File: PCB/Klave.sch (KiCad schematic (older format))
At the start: 78 parts, among them J1 6P6C, J2 OLED, SW0 Reset, SW1 0:0, SW10 1:3, SW11 1:4, SW12 1:5, SW13 2:0, SW14 2:1, SW15 2:2, SW16 2:3, SW17 2:4, SW18 2:5, SW19 3:0, SW2 0:1, SW20 3:1, SW21 3:2, SW22 3:3, SW23 3:4, SW24 3:5, SW26 4:1, SW27 4:2, SW28 4:3, SW29 4:4, SW3 0:2, SW30 4:5, SW35 5:4, SW36 5:5, SW4 0:3, SW5 0:4, SW6 0:5, SW7 1:0, SW8 1:1, SW9 1:2, U1 ProMicro

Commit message: Rename switch files
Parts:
- SW1, SW10, SW11, SW12, SW13, SW14, SW15, SW16, SW17, SW18, SW19, SW2, SW20, SW21, SW22, SW23, SW24, SW26, SW27, SW28, SW29, SW3, SW30, SW35, SW36, SW4, SW5, SW6, SW7, SW8, SW9: footprint KlaveLib:Kailh_MX_Socket -> KlaveLib:SW_Socket_MX
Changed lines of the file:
@@
 F 0 "SW2" H 7550 1900 50  0000 C CNN
 F 1 "0:1" H 7550 1600 50  0000 C CNB
-F 2 "KlaveLib:Kailh_MX_Socket" H 7550 1900 50  0001 C CNN
+F 2 "KlaveLib:SW_Socket_MX" H 7550 1900 50  0001 C CNN
 F 3 "~" H 7550 1900 50  0001 C CNN
 	1    7550 1700
@@
 F 0 "SW3" H 8250 1900 50  0000 C CNN
 F 1 "0:2" H 8250 1600 50  0000 C CNB
-F 2 "KlaveLib:Kailh_MX_Socket" H 8250 1900 50  0001 C CNN
+F 2 "KlaveLib:SW_Socket_MX" H 8250 1900 50  0001 C CNN
 F 3 "~" H 8250 1900 50  0001 C CNN
 	1    8250 1700
@@
 F 0 "SW4" H 8950 1900 50  0000 C CNN
 F 1 "0:3" H 8950 1600 50  0000 C CNB
-F 2 "KlaveLib:Kailh_MX_Socket" H 8950 1900 50  0001 C CNN
+F 2 "KlaveLib:SW_Socket_MX" H 8950 1900 50  0001 C CNN
 F 3 "~" H 8950 1900 50  0001 C CNN
 	1    8950 1700
@@
 F 0 "SW5" H 9650 1900 50  0000 C CNN
 F 1 "0:4" H 9650 1600 50  0000 C CNB
-F 2 "KlaveLib:Kailh_MX_Socket" H 9650 1900 50  0001 C CNN
+F 2 "KlaveLib:SW_Socket_MX" H 9650 1900 50  0001 C CNN
 F 3 "~" H 9650 1900 50  0001 C CNN
 	1    9650 1700
@@
 F 0 "SW6" H 10350 1900 50  0000 C CNN
 F 1 "0:5" H 10350 1600 50  0000 C CNB
-F 2 "KlaveLib:Kailh_MX_Socket" H 10350 1900 50  0001 C CNN
+F 2 "KlaveLib:SW_Socket_MX" H 10350 1900 50  0001 C CNN
 F 3 "~" H 10350 1900 50  0001 C CNN
 	1    10350 1700
@@
 F 0 "SW24" H 10350 3550 50  0000 C CNN
 F 1 "3:5" H 10350 3250 50  0000 C CNB
-F 2 "KlaveLib:Kailh_MX_Socket" H 10350 3550 50  0001 C CNN
+F 2 "KlaveLib:SW_Socket_MX" H 10350 3550 50  0001 C CNN
 F 3 "~" H 10350 3550 50  0001 C CNN
 	1    10350 3350
@@
 F 0 "SW12" H 10350 2450 50  0000 C CNN
 F 1 "1:5" H 10350 2150 50  0000 C CNB
-F 2 "KlaveLib:Kailh_MX_Socket" H 10350 2450 50  0001 C CNN
+F 2 "KlaveLib:SW_Socket_MX" H 10350 2450 50  0001 C CNN
 F 3 "~" H 10350 2450 50  0001 C CNN
 	1    10350 2250
@@
 F 0 "SW23" H 9650 3550 50  0000 C CNN
 F 1 "3:4" H 9650 3250 50  0000 C CNB
-F 2 "KlaveLib:Kailh_MX_Socket" H 9650 3550 50  0001 C CNN
+F 2 "KlaveLib:SW_Socket_MX" H 9650 3550 50  0001 C CNN
 F 3 "~" H 9650 3550 50  0001 C CNN
 	1    9650 3350
@@
 F 0 "SW17" H 9650 3000 50  0000 C CNN
 F 1 "2:4" H 9650 2700 50  0000 C CNB
-F 2 "KlaveLib:Kailh_MX_Socket" H 9650 3000 50  0001 C CNN
+F 2 "KlaveLib:SW_Socket_MX" H 9650 3000 50  0001 C CNN
 F 3 "~" H 9650 3000 50  0001 C CNN
 	1    9650 2800
@@
 F 0 "SW11" H 9650 2450 50  0000 C CNN
 F 1 "1:4" H 9650 2150 50  0000 C CNB
-F 2 "KlaveLib:Kailh_MX_Socket" H 9650 2450 50  0001 C CNN
+F 2 "KlaveLib:SW_Socket_MX" H 9650 2450 50  0001 C CNN
 F 3 "~" H 9650 2450 50  0001 C CNN
 	1    9650 2250
@@
 F 0 "SW22" H 8950 3550 50  0000 C CNN
 F 1 "3:3" H 8950 3250 50  0000 C CNB
-F 2 "KlaveLib:Kailh_MX_Socket" H 8950 3550 50  0001 C CNN
+F 2 "KlaveLib:SW_Socket_MX" H 8950 3550 50  0001 C CNN
 F 3 "~" H 8950 3550 50  0001 C CNN
 	1    8950 3350
@@
 F 0 "SW16" H 8950 3000 50  0000 C CNN
 F 1 "2:3" H 8950 2700 50  0000 C CNB
-F 2 "KlaveLib:Kailh_MX_Socket" H 8950 3000 50  0001 C CNN
+F 2 "KlaveLib:SW_Socket_MX" H 8950 3000 50  0001 C CNN
 F 3 "~" H 8950 3000 50  0001 C CNN
 	1    8950 2800
@@
 F 0 "SW10" H 8950 2450 50  0000 C CNN
 F 1 "1:3" H 8950 2150 50  0000 C CNB
-F 2 "KlaveLib:Kailh_MX_Socket" H 8950 2450 50  0001 C CNN
+F 2 "KlaveLib:SW_Socket_MX" H 8950 2450 50  0001 C CNN
 F 3 "~" H 8950 2450 50  0001 C CNN
 	1    8950 2250
@@
 F 0 "SW21" H 8250 3550 50  0000 C CNN
 F 1 "3:2" H 8250 3250 50  0000 C CNB
-F 2 "KlaveLib:Kailh_MX_Socket" H 8250 3550 50  0001 C CNN
+F 2 "KlaveLib:SW_Socket_MX" H 8250 3550 50  0001 C CNN
 F 3 "~" H 8250 3550 50  0001 C CNN
 	1    8250 3350
@@
 F 0 "SW15" H 8250 3000 50  0000 C CNN
 F 1 "2:2" H 8250 2700 50  0000 C CNB
-F 2 "KlaveLib:Kailh_MX_Socket" H 8250 3000 50  0001 C CNN
+F 2 "KlaveLib:SW_Socket_MX" H 8250 3000 50  0001 C CNN
 F 3 "~" H 8250 3000 50  0001 C CNN
 	1    8250 2800
@@
 F 0 "SW20" H 7550 3550 50  0000 C CNN
 F 1 "3:1" H 7550 3250 50  0000 C CNB
-F 2 "KlaveLib:Kailh_MX_Socket" H 7550 3550 50  0001 C CNN
+F 2 "KlaveLib:SW_Socket_MX" H 7550 3550 50  0001 C CNN
 F 3 "~" H 7550 3550 50  0001 C CNN
 	1    7550 3350
@@
 F 0 "SW14" H 7550 3000 50  0000 C CNN
 F 1 "2:1" H 7550 2700 50  0000 C CNB
-F 2 "KlaveLib:Kailh_MX_Socket" H 7550 3000 50  0001 C CNN
+F 2 "KlaveLib:SW_Socket_MX" H 7550 3000 50  0001 C CNN
 F 3 "~" H 7550 3000 50  0001 C CNN
 	1    7550 2800
@@
 F 0 "SW8" H 7550 2450 50  0000 C CNN
 F 1 "1:1" H 7550 2150 50  0000 C CNB
-F 2 "KlaveLib:Kailh_MX_Socket" H 7550 2450 50  0001 C CNN
+F 2 "KlaveLib:SW_Socket_MX" H 7550 2450 50  0001 C CNN
 F 3 "~" H 7550 2450 50  0001 C CNN
 	1    7550 2250
@@
 F 0 "SW19" H 6850 3550 50  0000 C CNN
 F 1 "3:0" H 6850 3250 50  0000 C CNB
-F 2 "KlaveLib:Kailh_MX_Socket" H 6850 3550 50  0001 C CNN
+F 2 "KlaveLib:SW_Socket_MX" H 6850 3550 50  0001 C CNN
 F 3 "~" H 6850 3550 50  0001 C CNN
 	1    6850 3350
@@
 F 0 "SW13" H 6850 3000 50  0000 C CNN
 F 1 "2:0" H 6850 2700 50  0000 C CNB
-F 2 "KlaveLib:Kailh_MX_Socket" H 6850 3000 50  0001 C CNN
+F 2 "KlaveLib:SW_Socket_MX" H 6850 3000 50  0001 C CNN
 F 3 "~" H 6850 3000 50  0001 C CNN
 	1    6850 2800
@@
 F 0 "SW7" H 6850 2450 50  0000 C CNN
 F 1 "1:0" H 6850 2150 50  0000 C CNB
-F 2 "KlaveLib:Kailh_MX_Socket" H 6850 2450 50  0001 C CNN
+F 2 "KlaveLib:SW_Socket_MX" H 6850 2450 50  0001 C CNN
 F 3 "~" H 6850 2450 50  0001 C CNN
 	1    6850 2250
@@
 F 0 "SW18" H 10350 3000 50  0000 C CNN
 F 1 "2:5" H 10350 2700 50  0000 C CNB
-F 2 "KlaveLib:Kailh_MX_Socket" H 10350 3000 50  0001 C CNN
+F 2 "KlaveLib:SW_Socket_MX" H 10350 3000 50  0001 C CNN
 F 3 "~" H 10350 3000 50  0001 C CNN
 	1    10350 2800
@@
 F 0 "SW30" H 10350 4100 50  0000 C CNN
 F 1 "4:5" H 10350 3800 50  0000 C CNB
-F 2 "KlaveLib:Kailh_MX_Socket" H 10350 4100 50  0001 C CNN
+F 2 "KlaveLib:SW_Socket_MX" H 10350 4100 50  0001 C CNN
 F 3 "~" H 10350 4100 50  0001 C CNN
 	1    10350 3900
@@
 F 0 "SW29" H 9650 4100 50  0000 C CNN
 F 1 "4:4" H 9650 3800 50  0000 C CNB
-F 2 "KlaveLib:Kailh_MX_Socket" H 9650 4100 50  0001 C CNN
+F 2 "KlaveLib:SW_Socket_MX" H 9650 4100 50  0001 C CNN
 F 3 "~" H 9650 4100 50  0001 C CNN
 	1    9650 3900
@@
 F 0 "SW28" H 8950 4100 50  0000 C CNN
 F 1 "4:3" H 8950 3800 50  0000 C CNB
-F 2 "KlaveLib:Kailh_MX_Socket" H 8950 4100 50  0001 C CNN
+F 2 "KlaveLib:SW_Socket_MX" H 8950 4100 50  0001 C CNN
 F 3 "~" H 8950 4100 50  0001 C CNN
 	1    8950 3900
@@
 F 0 "SW27" H 8250 4100 50  0000 C CNN
 F 1 "4:2" H 8250 3800 50  0000 C CNB
-F 2 "KlaveLib:Kailh_MX_Socket" H 8250 4100 50  0001 C CNN
+F 2 "KlaveLib:SW_Socket_MX" H 8250 4100 50  0001 C CNN
 F 3 "~" H 8250 4100 50  0001 C CNN
 	1    8250 3900
@@
 F 0 "SW26" H 7550 4100 50  0000 C CNN
 F 1 "4:1" H 7550 3800 50  0000 C CNB
-F 2 "KlaveLib:Kailh_MX_Socket" H 7550 4100 50  0001 C CNN
+F 2 "KlaveLib:SW_Socket_MX" H 7550 4100 50  0001 C CNN
 F 3 "~" H 7550 4100 50  0001 C CNN
 	1    7550 3900
@@
 F 0 "SW36" H 10350 4650 50  0000 C CNN
 F 1 "5:5" H 10350 4350 50  0000 C CNB
-F 2 "KlaveLib:Kailh_MX_Socket" H 10350 4650 50  0001 C CNN
+F 2 "KlaveLib:SW_Socket_MX" H 10350 4650 50  0001 C CNN
 F 3 "~" H 10350 4650 50  0001 C CNN
 	1    10350 4450
@@
 F 0 "SW35" H 9650 4650 50  0000 C CNN
 F 1 "5:4" H 9650 4350 50  0000 C CNB
-F 2 "KlaveLib:Kailh_MX_Socket" H 9650 4650 50  0001 C CNN
+F 2 "KlaveLib:SW_Socket_MX" H 9650 4650 50  0001 C CNN
 F 3 "~" H 9650 4650 50  0001 C CNN
 	1    9650 4450
@@
 F 0 "SW9" H 8250 2450 50  0000 C CNN
 F 1 "1:2" H 8250 2150 50  0000 C CNB
-F 2 "KlaveLib:Kailh_MX_Socket" H 8250 2450 50  0001 C CNN
+F 2 "KlaveLib:SW_Socket_MX" H 8250 2450 50  0001 C CNN
 F 3 "~" H 8250 2450 50  0001 C CNN
 	1    8250 2250
@@
 F 0 "SW1" H 6850 1900 50  0000 C CNN
 F 1 "0:0" H 6850 1600 50  0000 C CNB
-F 2 "KlaveLib:Kailh_MX_Socket" H 6850 1900 50  0001 C CNN
+F 2 "KlaveLib:SW_Socket_MX" H 6850 1900 50  0001 C CNN
 F 3 "~" H 6850 1900 50  0001 C CNN
 	1    6850 1700

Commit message: Apply schematic "best practices"
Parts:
- renumbered JP4 to JP1, JP3 to JP2, JP2 to JP3, JP1 to JP4
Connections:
- net GND: now also J1.6; no longer J1.5
- net VCC: now also J1.5; no longer J1.6
- net at J2.1 (Pin_1), JP1.1: now also JP5.1; no longer JP8.1
- net at J2.2 (Pin_2), JP2.1: now also JP6.1; no longer JP7.1
- net at J2.3 (Pin_3), JP3.1: now also JP7.1; no longer JP6.1
- net at J2.4 (Pin_4), JP4.1: now also JP8.1; no longer JP5.1
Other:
- moved on the sheet: J1, J2, JP1, JP2, JP3, JP4, JP5, JP6, JP7, JP8

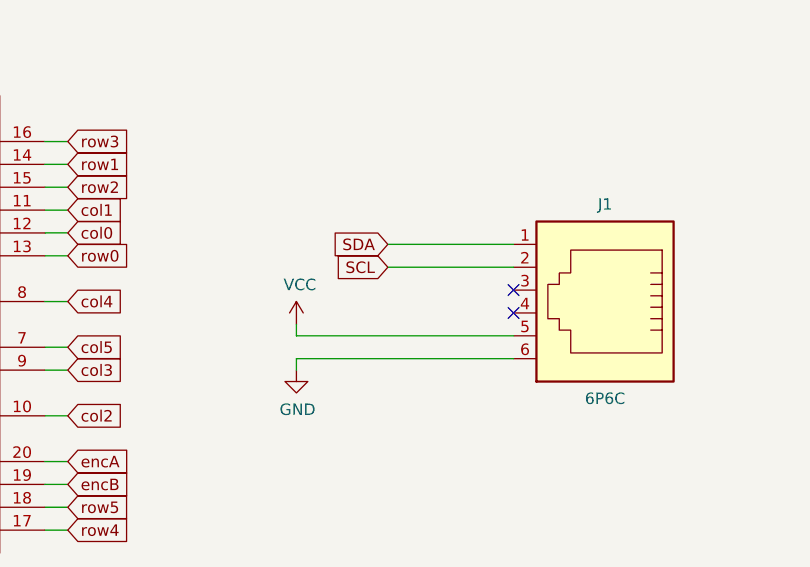
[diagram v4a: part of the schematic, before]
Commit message: Add connector protective resistors
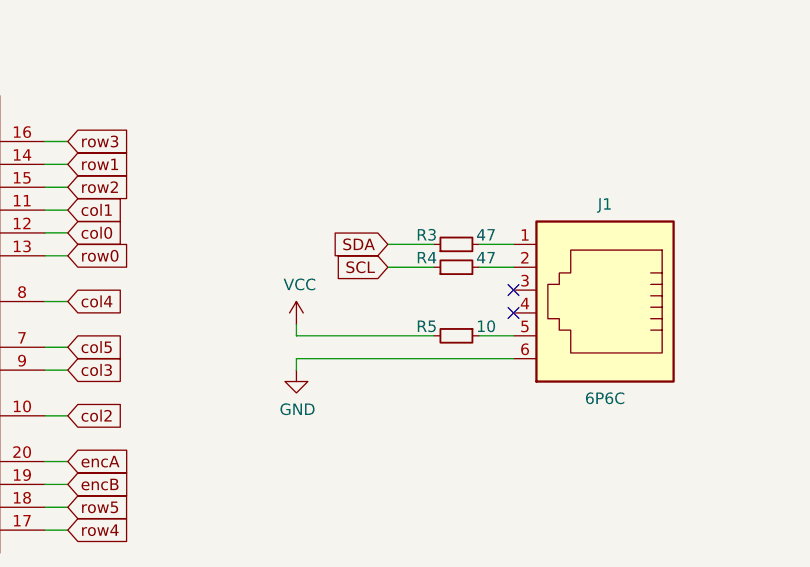
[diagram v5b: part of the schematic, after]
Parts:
- added R3, R4: 47, KlaveLib:R_Axial_DIN0207_L6.3mm_D2.5mm_P10.16mm_Horizontal, symbol Device:R_Small
- added R5: 10, KlaveLib:R_Axial_DIN0207_L6.3mm_D2.5mm_P10.16mm_Horizontal, symbol Device:R_Small
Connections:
- net SCL: now also R4.1; no longer J1.2
- net SDA: now also R3.1; no longer J1.1
- net VCC: now also R5.2; no longer J1.5
- new net: J1.1, R3.2
- new net: J1.2, R4.2
- new net: J1.5, R5.1
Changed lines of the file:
@@
 SDA
 $Comp
-L power:VCC #PWR?
+L power:VCC #PWR0106
 U 1 1 5F809260
 P 1250 6500
-F 0 "#PWR?" H 1250 6350 50  0001 C CNN
+F 0 "#PWR0106" H 1250 6350 50  0001 C CNN
 F 1 "VCC" H 1265 6673 50  0000 C CNN
 F 2 "" H 1250 6500 50  0001 C CNN
@@
 	1250 6500 1675 6500
 $Comp
-L power:VCC #PWR?
+L power:VCC #PWR0107
 U 1 1 5F815101
 P 1250 7150
-F 0 "#PWR?" H 1250 7000 50  0001 C CNN
+F 0 "#PWR0107" H 1250 7000 50  0001 C CNN
 F 1 "VCC" H 1265 7323 50  0000 C CNN
 F 2 "" H 1250 7150 50  0001 C CNN
@@
 	1250 7150 1675 7150
 $Comp
-L power:GND #PWR?
+L power:GND #PWR0109
 U 1 1 5F820E83
 P 1250 7250
-F 0 "#PWR?" H 1250 7000 50  0001 C CNN
+F 0 "#PWR0109" H 1250 7000 50  0001 C CNN
 F 1 "GND" H 1255 7077 50  0000 C CNN
 F 2 "" H 1250 7250 50  0001 C CNN
@@
 $EndComp
 $Comp
-L power:GND #PWR?
+L power:GND #PWR0110
 U 1 1 5F82211E
 P 1250 6600
-F 0 "#PWR?" H 1250 6350 50  0001 C CNN
+F 0 "#PWR0110" H 1250 6350 50  0001 C CNN
 F 1 "GND" H 1255 6427 50  0000 C CNN
 F 2 "" H 1250 6600 50  0001 C CNN
@@
 	2050 6950 2125 6950
 Wire Wire Line
-	3500 2250 4450 2250
+	4450 1850 4300 1850
 Wire Wire Line
-	3900 1950 4450 1950
+	4450 1950 4300 1950
 Wire Wire Line
-	3900 1850 4450 1850
+	4300 2250 4450 2250
+Wire Wire Line
+	3500 2250 4100 2250
+$Comp
+L Device:R_Small R5
+U 1 1 5F53C2AE
+P 4200 2250
+F 0 "R5" V 4160 2120 50  0000 C CNN
+F 1 "10" V 4160 2380 50  0000 C CNN
+F 2 "KlaveLib:R_Axial_DIN0207_L6.3mm_D2.5mm_P10.16mm_Horizontal" H 4200 2250 50  0001 C CNN
+F 3 "~" H 4200 2250 50  0001 C CNN
+	1    4200 2250
+	0    1    1    0
+$EndComp
+Wire Wire Line
+	4100 1850 3900 1850
+Wire Wire Line
+	3900 1950 4100 1950
+$Comp
+L Device:R_Small R4
+U 1 1 5F53B32E
+P 4200 1950
+F 0 "R4" V 4240 2080 50  0000 C CNN
+F 1 "47" V 4240 1820 50  0000 C CNN
+F 2 "KlaveLib:R_Axial_DIN0207_L6.3mm_D2.5mm_P10.16mm_Horizontal" H 4200 1950 50  0001 C CNN
+F 3 "~" H 4200 1950 50  0001 C CNN
+	1    4200 1950
+	0    -1   -1   0
+$EndComp
+$Comp
+L Device:R_Small R3
+U 1 1 5F53C0E5
+P 4200 1850
+F 0 "R3" V 4240 1980 50  0000 C CNN
+F 1 "47" V 4240 1720 50  0000 C CNN
+F 2 "KlaveLib:R_Axial_DIN0207_L6.3mm_D2.5mm_P10.16mm_Horizontal" H 4200 1850 50  0001 C CNN
+F 3 "~" H 4200 1850 50  0001 C CNN
+	1    4200 1850
+	0    -1   -1   0
+$EndComp
 $EndSCHEMATC
